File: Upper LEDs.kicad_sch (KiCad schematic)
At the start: 28 parts

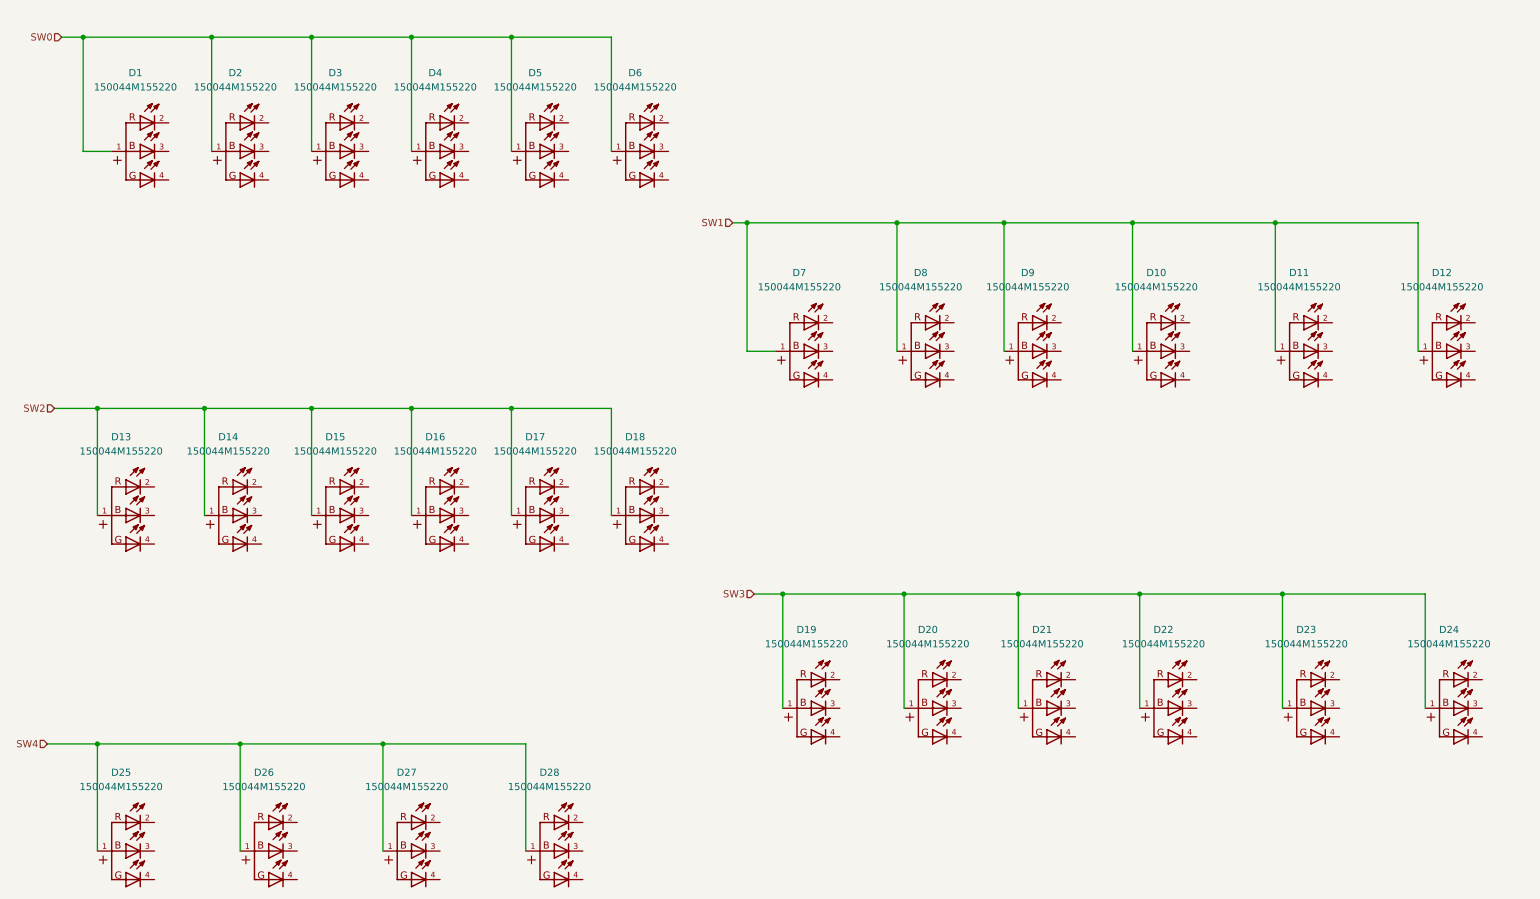
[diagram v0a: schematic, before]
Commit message: Initial complete implementation of LEDS.
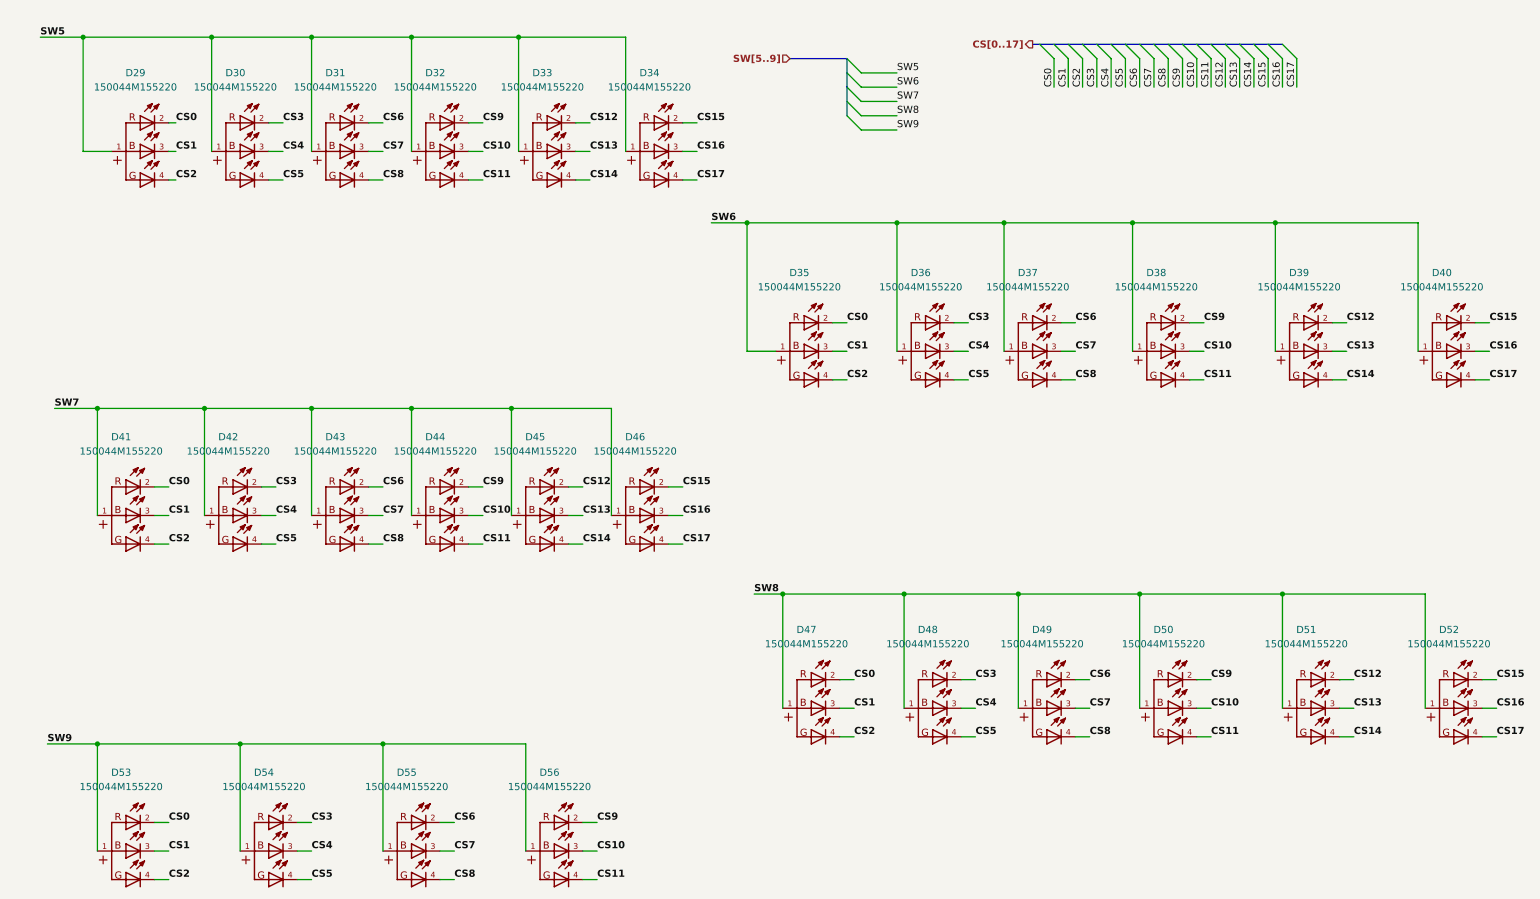
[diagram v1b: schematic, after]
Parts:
- renumbered D1 to D29, D2 to D30, D3 to D31, D4 to D32, D5 to D33, D6 to D34, D7 to D35, D8 to D36, D9 to D37, D10 to D38, D11 to D39, D12 to D40, D13 to D41, D14 to D42, D15 to D43, D16 to D44, D17 to D45, D18 to D46, D19 to D47, D20 to D48, D21 to D49, D22 to D50, D23 to D51, D24 to D52, D25 to D53, D26 to D54, D27 to D55, D28 to D56
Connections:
- net CS9: now reaches D56.2
- net CS9: now also D32.2, D38.2, D44.2, D50.2
- net CS10: now reaches D56.3
- net CS10: now also D32.3, D38.3, D44.3, D50.3
- net CS11: now reaches D56.4
- net CS11: now also D32.4, D38.4, D44.4, D50.4
- net CS12: now reaches D51.2
- net CS12: now also D33.2, D39.2, D45.2
- net CS13: now reaches D51.3
- net CS13: now also D33.3, D39.3, D45.3
- net CS14: now reaches D51.4
- net CS14: now also D33.4, D39.4, D45.4
- net CS3: now reaches D30.2
- net CS3: now also D36.2, D42.2, D48.2, D54.2
- net CS4: now reaches D30.3
- net CS4: now also D36.3, D42.3, D48.3, D54.3
- net CS5: now reaches D30.4
- net CS5: now also D36.4, D42.4, D48.4, D54.4
- net CS15: now reaches D34.2
- net CS15: now also D40.2, D46.2, D52.2
- net CS16: now reaches D34.3
- net CS16: now also D40.3, D46.3, D52.3
- net CS17: now reaches D34.4
- net CS17: now also D40.4, D46.4, D52.4
- net CS6: now reaches D31.2
- net CS6: now also D37.2, D43.2, D49.2, D55.2
- net CS7: now reaches D31.3
- net CS7: now also D37.3, D43.3, D49.3, D55.3
- net CS8: now reaches D31.4
- net CS8: now also D37.4, D43.4, D49.4, D55.4
- net CS0: now reaches D41.2
- net CS0: now also D29.2, D35.2, D47.2, D53.2
- net CS1: now reaches D41.3
- net CS1: now also D29.3, D35.3, D47.3, D53.3
- net CS2: now reaches D41.4
- net CS2: now also D29.4, D35.4, D47.4, D53.4
- net SW0 renamed SW5
- net SW1 renamed SW6
- net SW2 renamed SW7
- net SW3 renamed SW8
- net SW4 renamed SW9
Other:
- moved on the sheet: D33, D34

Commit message: First complete schematic with TPs.
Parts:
- added TP26, TP27, TP28, TP29, TP30: TestPoint, TestPoint:TestPoint_Pad_D1.0mm, symbol Connector:TestPoint
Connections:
- net SW5: now also TP26.1
- net SW6: now also TP27.1
- net SW7: now also TP28.1
- net SW8: now also TP29.1
- net SW9: now also TP30.1

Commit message: Re-annotated entire schematic.
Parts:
- renumbered TP26 to TP29, TP27 to TP30, TP28 to TP31, TP29 to TP32, TP30 to TP33
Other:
- title: (none) -> Hourglass
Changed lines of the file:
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@@
 	(generator_version "9.0")
 	(paper "A4")
+	(title_block
+		(title "Hourglass")
+		(date "2025-04-23")
+		(rev "01")
+	)
 	(junction
 		(at 212.09 116.84)
@@
 		(dnp no)
 		(fields_autoplaced yes)
-		(property "Reference" "TP26"
+		(property "Reference" "TP29"
 			(at 26.67 14.4779 0)
 			(effects
@@
 			(project "Hourglass_PCBA"
 				(path "/a75630d2-15a7-42bc-8ce0-7846cbd1da6b/9c708963-e8cc-42a5-9c83-1e957695e1ca/b9a46344-017d-4264-848c-625aefba8eb9"
-					(reference "TP26")
+					(reference "TP29")
 					(unit 1)
 				)
@@
 		(dnp no)
 		(fields_autoplaced yes)
-		(property "Reference" "TP29"
+		(property "Reference" "TP32"
 			(at 151.13 113.5379 0)
 			(effects
@@
 			(project "Hourglass_PCBA"
 				(path "/a75630d2-15a7-42bc-8ce0-7846cbd1da6b/9c708963-e8cc-42a5-9c83-1e957695e1ca/b9a46344-017d-4264-848c-625aefba8eb9"
-					(reference "TP29")
+					(reference "TP32")
 					(unit 1)
 				)
@@
 		(dnp no)
 		(fields_autoplaced yes)
-		(property "Reference" "TP27"
+		(property "Reference" "TP30"
 			(at 144.78 47.4979 0)
 			(effects
@@
 			(project "Hourglass_PCBA"
 				(path "/a75630d2-15a7-42bc-8ce0-7846cbd1da6b/9c708963-e8cc-42a5-9c83-1e957695e1ca/b9a46344-017d-4264-848c-625aefba8eb9"
-					(reference "TP27")
+					(reference "TP30")
 					(unit 1)
 				)
@@
 		(dnp no)
 		(fields_autoplaced yes)
-		(property "Reference" "TP30"
+		(property "Reference" "TP33"
 			(at 29.21 140.2079 0)
 			(effects
@@
 			(project "Hourglass_PCBA"
 				(path "/a75630d2-15a7-42bc-8ce0-7846cbd1da6b/9c708963-e8cc-42a5-9c83-1e957695e1ca/b9a46344-017d-4264-848c-625aefba8eb9"
-					(reference "TP30")
+					(reference "TP33")
 					(unit 1)
 				)
@@
 		(dnp no)
 		(fields_autoplaced yes)
-		(property "Reference" "TP28"
+		(property "Reference" "TP31"
 			(at 29.21 80.5179 0)
 			(effects
@@
 			(project "Hourglass_PCBA"
 				(path "/a75630d2-15a7-42bc-8ce0-7846cbd1da6b/9c708963-e8cc-42a5-9c83-1e957695e1ca/b9a46344-017d-4264-848c-625aefba8eb9"
-					(reference "TP28")
+					(reference "TP31")
 					(unit 1)
 				)
